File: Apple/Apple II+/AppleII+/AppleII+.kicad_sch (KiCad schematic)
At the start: 0 parts

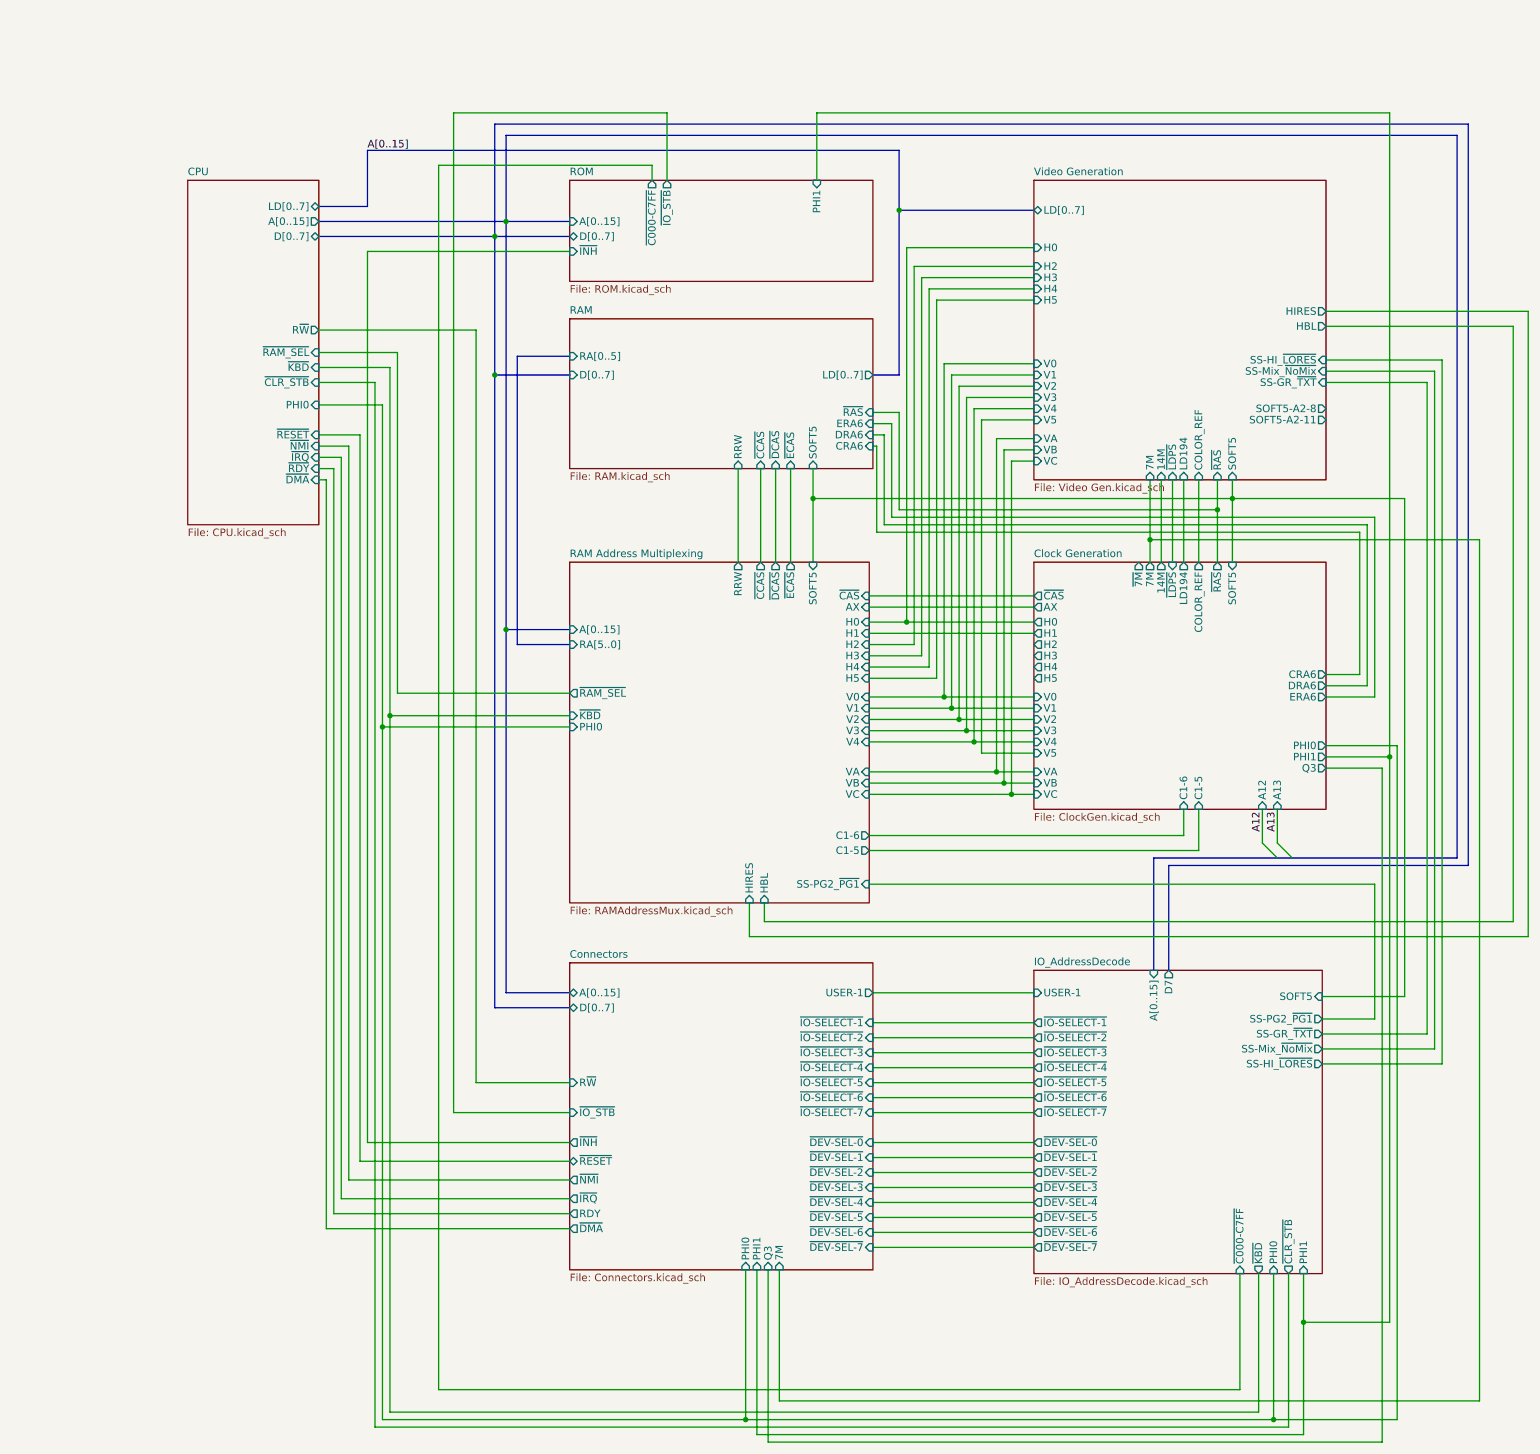
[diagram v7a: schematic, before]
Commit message: Changed SOFT5-A2-8 and -11 to just SOFT5, based on Apple II Circuit Description Book
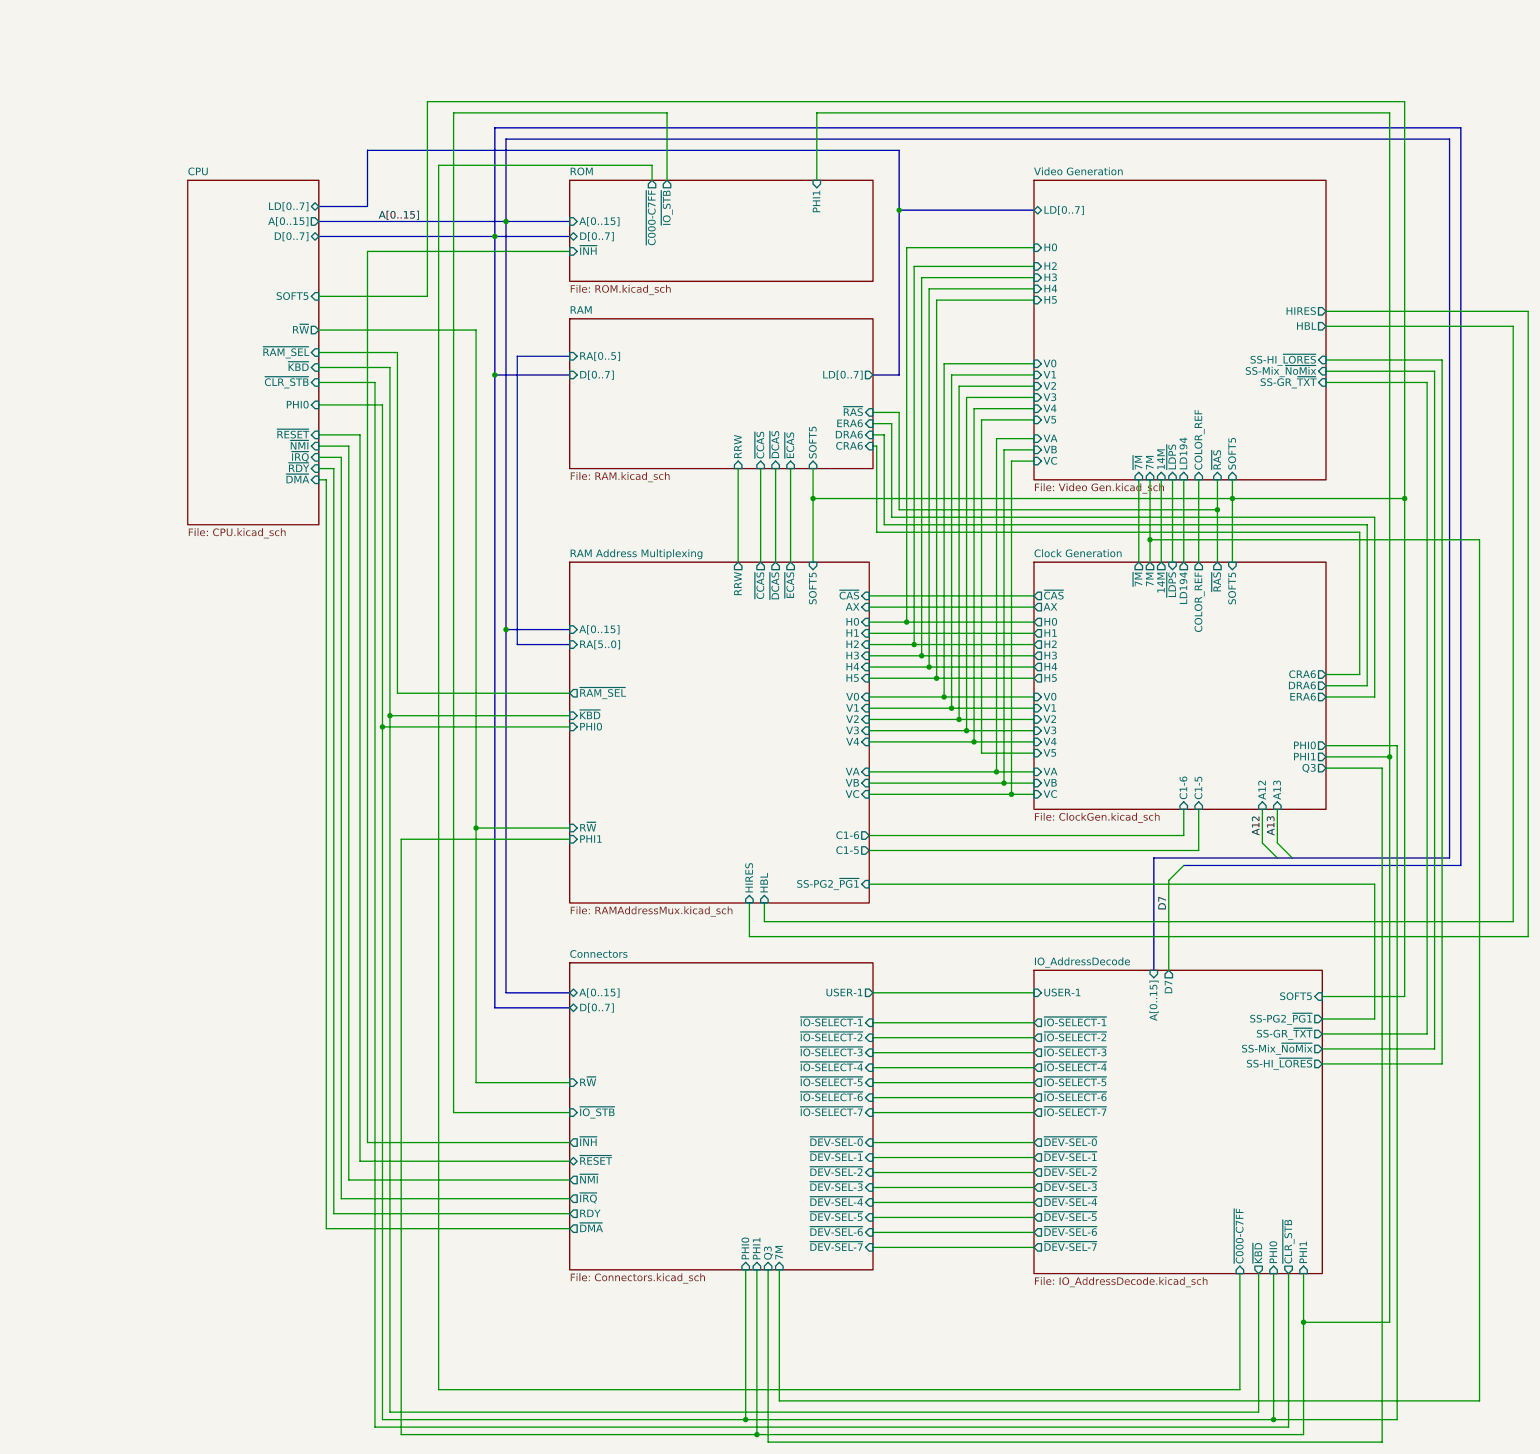
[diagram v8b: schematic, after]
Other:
- sheet CPU ports: added SOFT5; removed none
- sheet RAM Address Multiplexing ports: added PHI1, R~{W}; removed none
- sheet Video Generation ports: added ~{7M}; removed SOFT5-A2-11, SOFT5-A2-8
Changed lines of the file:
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@@
   (junction (at 192.405 144.78) (diameter 0) (color 0 0 0 0)
   )
+  (junction (at 182.245 128.905) (diameter 0) (color 0 0 0 0)
+  )
   (junction (at 232.41 98.425) (diameter 0) (color 0 0 0 0)
   )
   (junction (at 218.44 105.41) (diameter 0) (color 0 0 0 0)
   )
+  (junction (at 180.975 127) (diameter 0) (color 0 0 0 0)
+  )
   (junction (at 259.08 142.24) (diameter 0) (color 0 0 0 0)
   )
@@
   (junction (at 107.315 53.975) (diameter 0) (color 0 0 0 0)
   )
+  (junction (at 178.435 123.19) (diameter 0) (color 0 0 0 0)
+  )
+  (junction (at 104.14 154.305) (diameter 0) (color 0 0 0 0)
+  )
   (junction (at 239.395 254.635) (diameter 0) (color 0 0 0 0)
   )
+  (junction (at 261.62 98.425) (diameter 0) (color 0 0 0 0)
+  )
   (junction (at 188.595 139.7) (diameter 0) (color 0 0 0 0)
   )
+  (junction (at 151.765 257.175) (diameter 0) (color 0 0 0 0)
+  )
+  (junction (at 179.705 125.095) (diameter 0) (color 0 0 0 0)
+  )
   (junction (at 109.22 120.65) (diameter 0) (color 0 0 0 0)
   )
@@
     (stroke (width 0) (type default))
   )
+  (bus_entry (at 221.615 163.195) (size 2.54 -2.54)
+    (stroke (width 0) (type default))
+  )
   (bus_entry (at 240.03 156.845) (size 2.54 2.54)
     (stroke (width 0) (type default))
@@
     (stroke (width 0) (type default))
   )
-  (bus (pts (xy 270.51 36.83) (xy 270.51 159.385))
+  (wire (pts (xy 104.14 69.85) (xy 104.14 154.305))
+    (stroke (width 0) (type default))
+  )
+  (bus (pts (xy 269.24 37.465) (xy 269.24 159.385))
     (stroke (width 0) (type default))
   )
@@
     (stroke (width 0) (type default))
   )
+  (wire (pts (xy 180.975 127) (xy 198.755 127))
+    (stroke (width 0) (type default))
+  )
   (wire (pts (xy 149.86 229.235) (xy 149.86 254.635))
     (stroke (width 0) (type default))
@@
     (stroke (width 0) (type default))
   )
-  (wire (pts (xy 104.14 197.485) (xy 104.14 69.85))
-    (stroke (width 0) (type default))
-  )
   (bus (pts (xy 107.315 77.47) (xy 107.315 184.785))
     (stroke (width 0) (type default))
@@
     (stroke (width 0) (type default))
   )
+  (wire (pts (xy 91.44 156.21) (xy 91.44 257.175))
+    (stroke (width 0) (type default))
+  )
   (wire (pts (xy 136.525 33.02) (xy 136.525 44.45))
     (stroke (width 0) (type default))
@@
     (stroke (width 0) (type default))
   )
+  (wire (pts (xy 91.44 257.175) (xy 151.765 257.175))
+    (stroke (width 0) (type default))
+  )
   (bus (pts (xy 240.03 159.385) (xy 242.57 159.385))
     (stroke (width 0) (type default))
@@
     (stroke (width 0) (type default))
   )
-  (bus (pts (xy 221.615 160.655) (xy 221.615 178.435))
-    (stroke (width 0) (type default))
-  )
   (wire (pts (xy 97.79 41.91) (xy 97.79 249.555))
     (stroke (width 0) (type default))
@@
     (stroke (width 0) (type default))
   )
+  (wire (pts (xy 95.885 64.135) (xy 95.885 31.115))
+    (stroke (width 0) (type default))
+  )
   (wire (pts (xy 232.41 98.425) (xy 232.41 109.22))
     (stroke (width 0) (type default))
@@
     (stroke (width 0) (type default))
   )
-  (bus (pts (xy 221.615 160.655) (xy 272.415 160.655))
-    (stroke (width 0) (type default))
-  )
-  (bus (pts (xy 272.415 160.655) (xy 272.415 34.925))
+  (bus (pts (xy 271.145 160.655) (xy 271.145 35.56))
     (stroke (width 0) (type default))
   )
@@
     (stroke (width 0) (type default))
   )
+  (bus (pts (xy 224.155 160.655) (xy 271.145 160.655))
+    (stroke (width 0) (type default))
+  )
   (wire (pts (xy 90.805 73.66) (xy 90.805 131.445))
     (stroke (width 0) (type default))
@@
     (stroke (width 0) (type default))
   )
-  (bus (pts (xy 109.22 51.435) (xy 109.22 36.83))
+  (bus (pts (xy 109.22 51.435) (xy 109.22 37.465))
     (stroke (width 0) (type default))
   )
@@
     (stroke (width 0) (type default))
   )
-  (bus (pts (xy 272.415 34.925) (xy 107.315 34.925))
+  (bus (pts (xy 271.145 35.56) (xy 107.315 35.56))
+    (stroke (width 0) (type default))
+  )
+  (wire (pts (xy 120.015 156.21) (xy 91.44 156.21))
     (stroke (width 0) (type default))
   )
@@
     (stroke (width 0) (type default))
   )
+  (wire (pts (xy 179.705 125.095) (xy 198.755 125.095))
+    (stroke (width 0) (type default))
+  )
   (wire (pts (xy 154.94 93.345) (xy 154.94 109.22))
     (stroke (width 0) (type default))
@@
     (stroke (width 0) (type default))
   )
+  (wire (pts (xy 104.14 154.305) (xy 104.14 197.485))
+    (stroke (width 0) (type default))
+  )
   (wire (pts (xy 193.675 146.685) (xy 198.755 146.685))
     (stroke (width 0) (type default))
@@
     (stroke (width 0) (type default))
   )
-  (bus (pts (xy 242.57 159.385) (xy 270.51 159.385))
+  (bus (pts (xy 242.57 159.385) (xy 269.24 159.385))
     (stroke (width 0) (type default))
   )
@@
     (stroke (width 0) (type default))
   )
-  (bus (pts (xy 107.315 34.925) (xy 107.315 53.975))
+  (bus (pts (xy 107.315 35.56) (xy 107.315 53.975))
     (stroke (width 0) (type default))
   )
@@
     (stroke (width 0) (type default))
   )
+  (wire (pts (xy 95.885 31.115) (xy 261.62 31.115))
+    (stroke (width 0) (type default))
+  )
   (wire (pts (xy 171.45 182.245) (xy 198.755 182.245))
     (stroke (width 0) (type default))
@@
     (stroke (width 0) (type default))
   )
+  (wire (pts (xy 77.47 64.135) (xy 95.885 64.135))
+    (stroke (width 0) (type default))
+  )
   (wire (pts (xy 171.45 225.425) (xy 198.755 225.425))
     (stroke (width 0) (type default))
@@
     (stroke (width 0) (type default))
   )
+  (wire (pts (xy 216.535 95.25) (xy 216.535 109.22))
+    (stroke (width 0) (type default))
+  )
   (wire (pts (xy 86.995 78.74) (xy 86.995 255.905))
     (stroke (width 0) (type default))
   )
+  (wire (pts (xy 178.435 123.19) (xy 198.755 123.19))
+    (stroke (width 0) (type default))
+  )
   (wire (pts (xy 186.055 135.89) (xy 198.755 135.89))
     (stroke (width 0) (type default))
@@
     (stroke (width 0) (type default))
   )
+  (wire (pts (xy 261.62 31.115) (xy 261.62 98.425))
+    (stroke (width 0) (type default))
+  )
+  (wire (pts (xy 182.245 128.905) (xy 198.755 128.905))
+    (stroke (width 0) (type default))
+  )
   (wire (pts (xy 177.165 55.88) (xy 177.165 119.38))
     (stroke (width 0) (type default))
@@
     (stroke (width 0) (type default))
   )
+  (wire (pts (xy 170.815 155.575) (xy 224.155 155.575))
+    (stroke (width 0) (type default))
+  )
   (wire (pts (xy 161.925 33.02) (xy 259.08 33.02))
     (stroke (width 0) (type default))
@@
     (stroke (width 0) (type default))
   )
+  (wire (pts (xy 120.015 154.305) (xy 104.14 154.305))
+    (stroke (width 0) (type default))
+  )
   (wire (pts (xy 78.74 95.25) (xy 77.47 95.25))
     (stroke (width 0) (type default))
@@
     (stroke (width 0) (type default))
   )
-  (wire (pts (xy 170.815 155.575) (xy 224.155 155.575))
-    (stroke (width 0) (type default))
-  )
   (wire (pts (xy 226.695 158.115) (xy 226.695 151.13))
     (stroke (width 0) (type default))
   )
-  (bus (pts (xy 109.22 36.83) (xy 270.51 36.83))
+  (bus (pts (xy 109.22 37.465) (xy 269.24 37.465))
     (stroke (width 0) (type default))
   )
@@
     (stroke (width 0) (type default))
   )
+  (wire (pts (xy 221.615 163.195) (xy 221.615 178.435))
+    (stroke (width 0) (type default))
+  )
   (bus (pts (xy 120.015 184.785) (xy 107.315 184.785))
     (stroke (width 0) (type default))
@@
     (stroke (width 0) (type default))
   )
-  (label "A13" (at 240.03 154.94 90) (fields_autoplaced)
+  (label "A13" (at 240.03 155.575 90) (fields_autoplaced)
     (effects (font (size 1.27 1.27)) (justify left bottom))
   )
-  (label "A12" (at 237.49 154.94 90) (fields_autoplaced)
+  (label "A12" (at 237.49 155.575 90) (fields_autoplaced)
     (effects (font (size 1.27 1.27)) (justify left bottom))
   )
-  (label "A[0..15]" (at 85.725 39.37 0) (fields_autoplaced)
+  (label "D7" (at 221.615 168.275 90) (fields_autoplaced)
+    (effects (font (size 1.27 1.27)) (justify left bottom))
+  )
+  (label "A[0..15]" (at 87.63 51.435 0) (fields_autoplaced)
     (effects (font (size 1.27 1.27)) (justify left bottom))
   )
@@
       (effects (font (size 1.27 1.27)) (justify right))
     )
+    (pin "SOFT5" input (at 77.47 64.135 0)
+      (effects (font (size 1.27 1.27)) (justify right))
+    )
     (instances
       (project "AppleII+"
@@
       (effects (font (size 1.27 1.27)) (justify right))
     )
+    (pin "PHI1" input (at 120.015 156.21 180)
+      (effects (font (size 1.27 1.27)) (justify left))
+    )
+    (pin "R~{W}" input (at 120.015 154.305 180)
+      (effects (font (size 1.27 1.27)) (justify left))
+    )
     (instances
       (project "AppleII+"
@@
       (effects (font (size 1.27 1.27)) (justify left))
     )
-    (pin "SOFT5-A2-11" output (at 248.285 85.09 0)
-      (effects (font (size 1.27 1.27)) (justify right))
-    )
-    (pin "SOFT5-A2-8" output (at 248.285 83.185 0)
-      (effects (font (size 1.27 1.27)) (justify right))
-    )
     (pin "HIRES" output (at 248.285 66.675 0)
       (effects (font (size 1.27 1.27)) (justify right))
@@
       (effects (font (size 1.27 1.27)) (justify right))
     )
+    (pin "~{7M}" input (at 216.535 95.25 270)
+      (effects (font (size 1.27 1.27)) (justify left))
+    )
     (instances
